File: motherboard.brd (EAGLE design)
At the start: 177.1 x 75.9 mm, 188 parts, among them IC1 LM2576, IC10 TUSB2046B, IC12 LM50, IC13 LM50, IC2 74LS595D, IC3 74LS595D, IC4 IC_FT230X-SSOP-16, IC5 VN5772AK, IC6 VN5772AK, IC7 VN5772AK, IC8 VN5772AK, IC9 VN5772AK, U2 NCP4625, U3 ATMEGA168, Y1 16Mhz, Y2 6MHz

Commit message: laying out subsystems
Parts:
- moved D8 244.7 mm to (-247.7, 204.5), turned to 270 degrees
- moved JP2 242.3 mm to (-213.4, 219.7)
- moved JP3 241.3 mm to (-221.0, 219.7)
- moved JP4 240.3 mm to (-228.6, 219.7)
- moved JP5 239.3 mm to (-236.2, 219.7)
- moved JP6 238.3 mm to (-243.8, 219.7)
- moved D9 233.3 mm to (-247.7, 195.6), turned to 270 degrees
- moved C22 226.7 mm to (-243.2, 15.2), turned to 90 degrees
- moved IC9 223.9 mm to (-252.7, 171.4), turned to 270 degrees
- moved IC7 221.3 mm to (-214.6, 166.4)
- moved D10 221.0 mm to (-240.0, 204.5), turned to 270 degrees
- moved IC8 219.8 mm to (-231.1, 167.6)
- moved C9 214.5 mm to (-231.1, 24.1)
- moved IC1 214.1 mm to (-85.1, 214.6)
- moved U2 211.3 mm to (-240.0, 15.2)
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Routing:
- net GND: track 0.00 -> 107.7 mm, vias 0 -> 69
- net +12V: track 0.00 -> 95.9 mm, vias 0 -> 5
- net +5V: track 0.00 -> 33.4 mm
- net 3.3V: track 0.00 -> 20.4 mm
- net N$5: track 0.00 -> 19.6 mm
- net N$13: track 0.00 -> 19.6 mm
- net N$15: track 0.00 -> 19.6 mm
- net N$12: track 0.00 -> 19.6 mm
- net N$9: track 0.00 -> 19.6 mm
- net N$10: track 0.00 -> 17.2 mm
- net N$11: track 0.00 -> 17.2 mm
- net N$3: track 0.00 -> 17.1 mm
- net N$8: track 0.00 -> 17.1 mm
- net N$14: track 0.00 -> 17.1 mm
- net N$1: track 0.00 -> 9.35 mm
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- added copper zone on layer 1, net GND

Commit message: updated
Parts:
- added C43: 0.1uF, adafruit:C1206
- moved C52 223.6 mm to (-236.2, 29.5), turned to 180 degrees
- moved IC4 219.3 mm to (-236.2, 22.9), turned to 270 degrees
- moved R27 218.5 mm to (-231.1, 22.9), turned to 270 degrees
- moved C23 217.0 mm to (-241.3, 21.3), turned to 270 degrees
- moved R29 215.5 mm to (-236.2, 18.7), turned to 180 degrees
- moved R30 212.0 mm to (-236.2, 16.2), turned to 180 degrees
- moved R28 211.5 mm to (-228.6, 22.9), turned to 270 degrees
- moved C34 198.3 mm to (-236.2, 27.0), turned to 180 degrees
- moved R11 195.2 mm to (-200.0, 21.3)
- moved C32 171.4 mm to (-232.1, 17.5), turned to 270 degrees
- moved IC3 163.3 mm to (-132.1, 200.3), turned to 270 degrees
- moved C33 159.5 mm to (-229.9, 27.0), turned to 180 degrees
- moved C37 147.7 mm to (-132.1, 222.9), turned to 180 degrees
- moved C7 146.4 mm to (-132.1, 220.3), turned to 180 degrees
- moved U$13 144.8 mm to (-134.6, 47.0), turned to 180 degrees
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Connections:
- new net N$16: C43.2, IC4.2
- net !RST: now also C43.1; no longer IC4.2
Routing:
- net +5V: track 33.4 -> 127.4 mm, vias 0 -> 3
- net MISO: track 0.00 -> 30.9 mm
- net D1+: track 0.00 -> 30.9 mm, vias 0 -> 2
- net SCK: track 0.00 -> 30.7 mm
- net MOSI: track 0.00 -> 30.7 mm
- net D1-: track 0.00 -> 26.0 mm, vias 0 -> 2
- net N$26: track 0.00 -> 23.7 mm
- net N$27: track 0.00 -> 20.9 mm, vias 0 -> 2
- net AGND: track 0.00 -> 18.3 mm
- net GND: track 107.7 -> 90.2 mm
- net N$19: track 0.00 -> 13.3 mm
- net N$38: track 0.00 -> 9.87 mm
- net N$7: track 0.00 -> 9.27 mm
- net N$51: track 0.00 -> 8.29 mm
- net N$58: track 0.00 -> 8.29 mm
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
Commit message: rewired h-bridges to not short out and simplified trace layout
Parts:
- moved C21 271.8 mm to (-290.8, 135.9)
- moved C19 251.1 mm to (-261.6, 144.8)
- moved C11 240.6 mm to (-284.5, 231.1)
- moved C13 229.8 mm to (-276.9, 231.1)
- moved C40 208.3 mm to (-283.2, 135.9)
- moved C15 205.6 mm to (-284.5, 188.0)
- moved C42 194.7 mm to (-275.6, 135.9)
- moved C17 193.7 mm to (-276.9, 188.0)
- moved R7 144.7 mm to (-290.8, 224.8)
- moved C10 143.0 mm to (-288.3, 252.7)
- moved R8 137.4 mm to (-285.8, 224.8)
- moved ZD2 134.9 mm to (-290.8, 231.1)
- moved D20 115.2 mm to (-289.6, 118.1), turned to 0 degrees
- moved IC6 110.9 mm to (-284.5, 240.0), turned to 0 degrees
- moved R9 107.8 mm to (-285.8, 181.6)
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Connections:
- removed net N$15: C41.2, D8.A, D9.C, IC9.12, IC9.14, IC9.15, IC9.18, IC9.22, IC9.23, JP6.2
- new net N$59: C6.1, D2.A, D3.C, IC5.1, IC5.22, IC5.23, IC5.25, IC5.28, IC5.3, JP2.1
- net 1HA: now also IC7.2, IC7.8; no longer IC6.2, IC6.8
- net 1HB: now also IC7.13, IC7.7; no longer IC6.13, IC6.7
- net 1SENSE: now also R10.1, R9.2, ZD3.C; no longer R7.2, R8.1, ZD2.C
- net 1STAT: now also IC7.4; no longer IC6.4
- net 2HA: now also IC6.2, IC6.8; no longer IC7.2, IC7.8
- net 2HB: now also IC6.13, IC6.7; no longer IC7.13, IC7.7
- net 2SENSE: now also R7.2, R8.1, ZD2.C; no longer R10.1, R9.2, ZD3.C
- net 2STAT: now also IC6.4; no longer IC7.4
- net 3HA: now also IC9.2, IC9.8; no longer IC8.2, IC8.8
- net 3HB: now also IC9.13, IC9.7; no longer IC8.13, IC8.7
- net 3SENSE: now also R36.2, R37.1, ZD5.C; no longer R26.2, R31.1, ZD4.C
- net 3STAT: now also IC9.4; no longer IC8.4
- net 4HA: now also IC8.2, IC8.8; no longer IC9.2, IC9.8
- net 4HB: now also IC8.13, IC8.7; no longer IC9.13, IC9.7
- net 4SENSE: now also R26.2, R31.1, ZD4.C; no longer R36.2, R37.1, ZD5.C
- net 4STAT: now also IC8.4; no longer IC9.4
- net N$10: now also C20.2, D16.A, D17.C, IC8.12, IC8.14, IC8.15, IC8.18, JP5.2; no longer C20.1, D10.A, D11.C, IC8.1, IC8.25, IC8.28, IC8.3, JP5.1
- net N$11: now also C20.1, D14.A, D15.C, IC8.1, IC8.22, IC8.23, IC8.25, IC8.28, IC8.3, JP5.1; no longer C6.1, D2.A, D3.C, IC5.1, IC5.20, IC5.21, IC5.25, IC5.28, IC5.3, JP2.1
- net N$12: now also C41.2, D20.A, D21.C, IC9.12, IC9.14, IC9.15, IC9.18, IC9.20, IC9.21, JP6.2; no longer C20.2, D12.A, D13.C, IC8.12, IC8.14, IC8.15, IC8.18, IC8.22, IC8.23, JP5.2
- net N$13: now also IC5.20, IC5.21; no longer IC5.22, IC5.23
- net N$14: now also D18.A, D19.C, IC9.22, IC9.23; no longer D6.A, D7.C, IC9.20, IC9.21
- net N$3: now also C12.2, D8.A, D9.C, IC6.12, IC6.14, IC6.15, IC6.18, JP3.2; no longer C12.1, D18.A, D19.C, IC6.1, IC6.25, IC6.28, IC6.3, JP3.1
- net N$5: now also C12.1, D6.A, D7.C, IC6.1, IC6.25, IC6.28, IC6.3, JP3.1; no longer C12.2, D20.A, D21.C, IC6.12, IC6.14, IC6.15, IC6.18, JP3.2
- net N$8: now also C16.2, D12.A, D13.C, IC7.12, IC7.14, IC7.15, IC7.18, JP4.2; no longer C16.1, D14.A, D15.C, IC7.1, IC7.25, IC7.28, IC7.3, JP4.1
- net N$9: now also C16.1, D10.A, D11.C, IC7.1, IC7.25, IC7.28, IC7.3, JP4.1; no longer C16.2, D16.A, D17.C, IC7.12, IC7.14, IC7.15, IC7.18, JP4.2
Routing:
- net N$5: track 19.6 -> 0.00 mm
- net N$15: track 19.6 -> 0.00 mm
- net N$12: track 19.6 -> 0.00 mm
- net N$9: track 19.6 -> 0.00 mm
- net N$10: track 17.2 -> 0.00 mm
- net N$59: track 0.00 -> 17.2 mm
- net N$11: track 17.2 -> 0.00 mm
- net N$3: track 17.1 -> 0.00 mm
- net N$8: track 17.1 -> 0.00 mm
- net N$14: track 17.1 -> 0.00 mm
- net +12V: track 95.9 -> 79.4 mm
- net GND: track 90.2 -> 74.2 mm

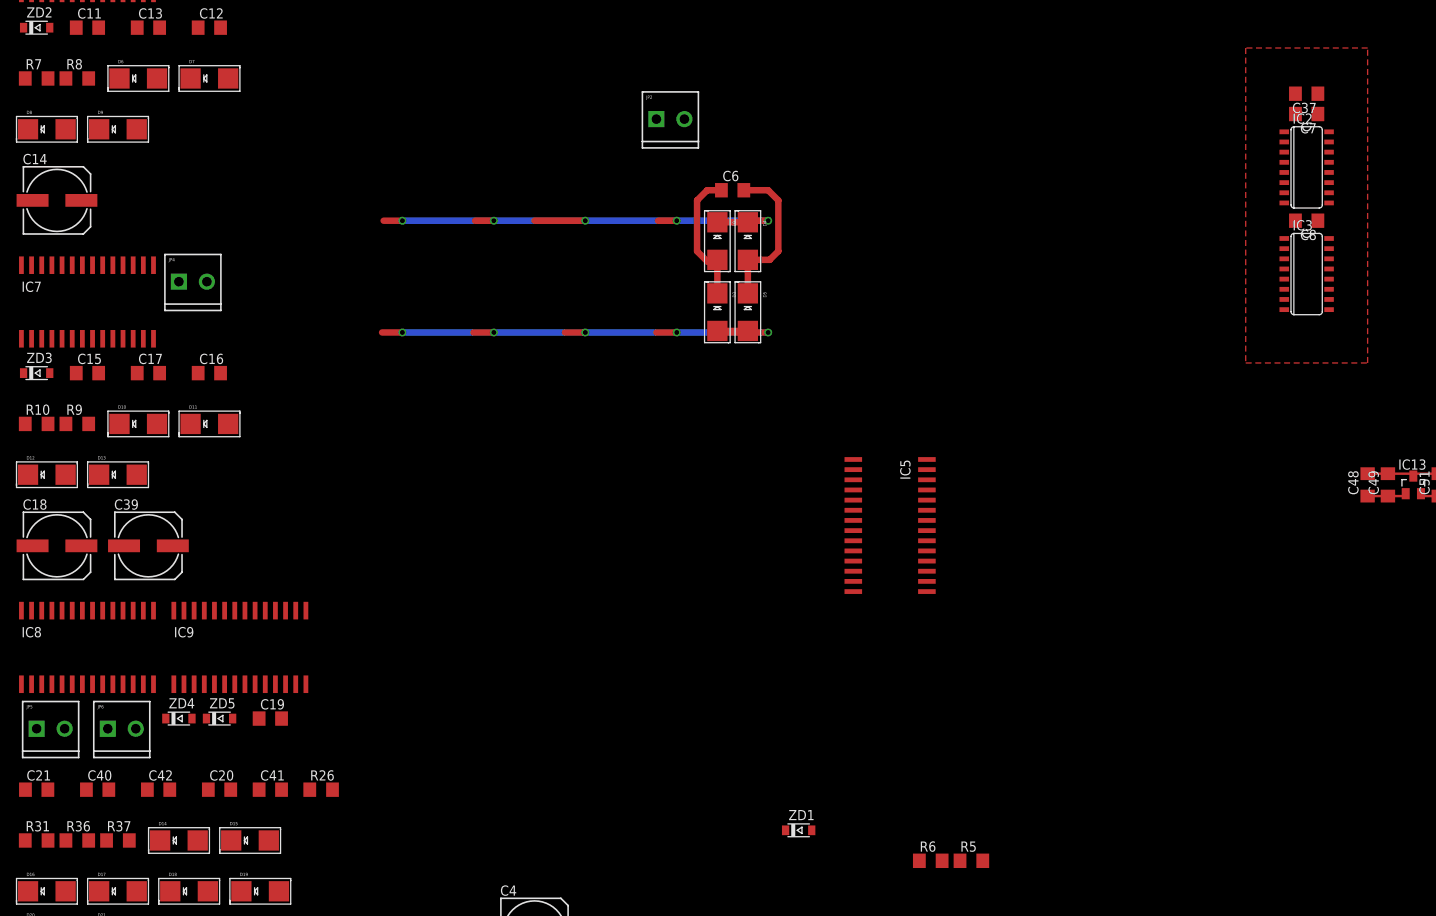
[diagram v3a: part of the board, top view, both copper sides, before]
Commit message: added current liminting resistors to shift registers
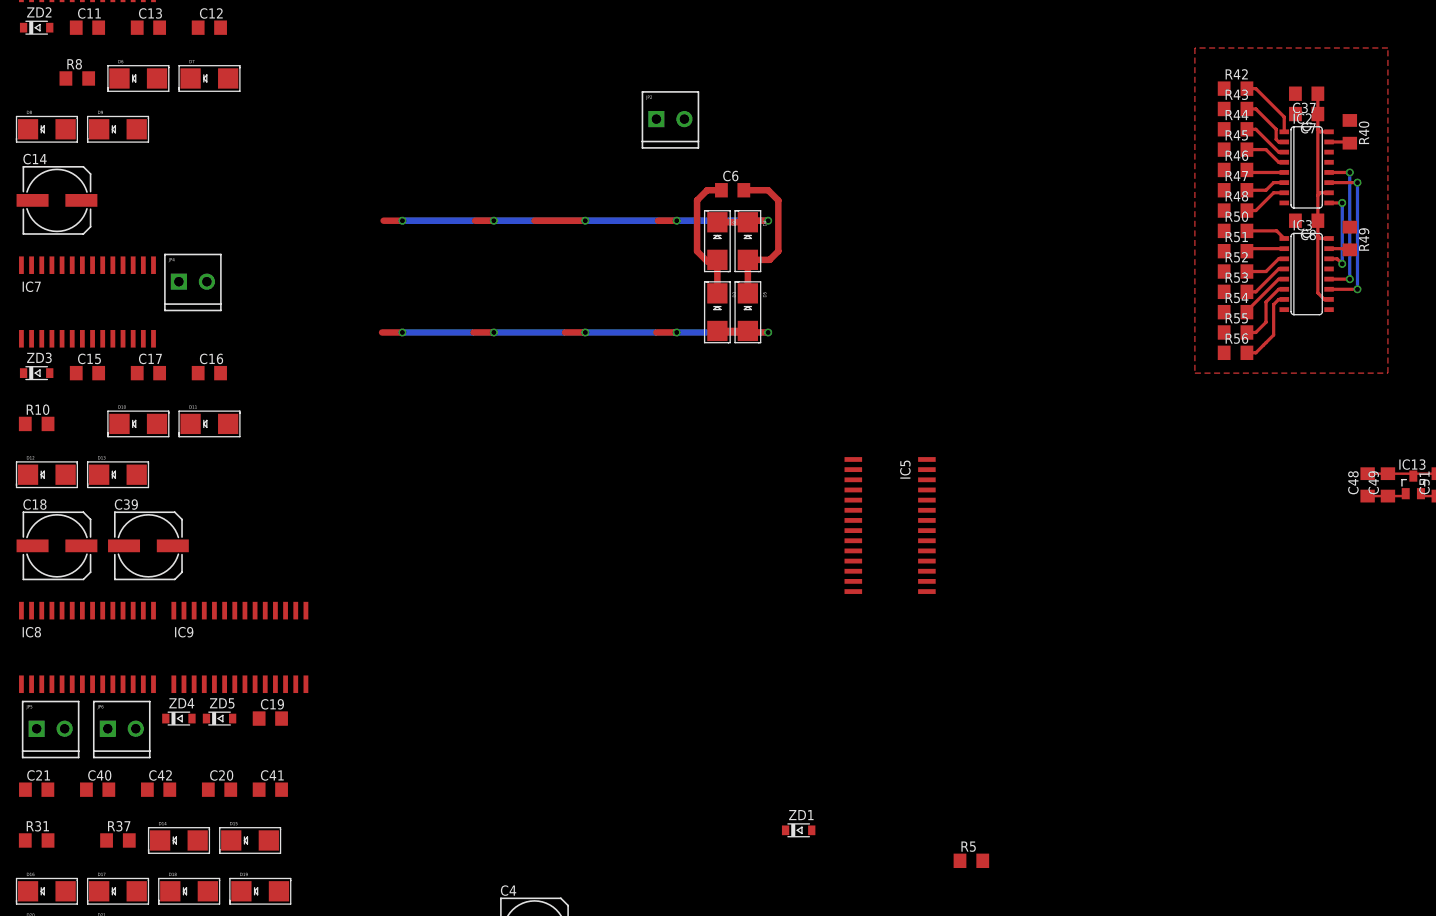
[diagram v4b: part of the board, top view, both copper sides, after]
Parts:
- removed R26, R36, R6, R7, R9: 1k, adafruit:R1206
- added R40, R42, R43, R44, R45, R46, R47, R48, R49, R50, R51, R52, R53, R54, R55, R56: 10k, adafruit:R1206
- R10, R31, R37, R5, R8: value 1k -> 2k
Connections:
- removed net 5HA: IC3.2
- removed net 5HB: IC3.3
- new net N$15: IC3.7, R56.2
- new net N$17: IC3.6, R55.2
- new net N$18: IC3.5, R54.2
- new net N$56: IC3.4, R53.2
- new net N$60: IC3.3, R52.2
- new net N$61: IC3.2, R51.2
- new net N$62: IC3.1, R50.2
- new net N$63: IC3.15, R49.2
- new net N$64: IC2.7, R48.2
- new net N$65: IC2.6, R47.2
- new net N$66: IC2.5, R46.2
- new net N$67: IC2.4, R45.2
- new net N$68: IC2.3, R44.2
- new net N$69: IC2.2, R43.2
- new net N$70: IC2.1, R42.2
- new net N$71: IC2.15, R40.2
- new net SW4: R54.1, R55.1
- new net SW5: R56.1
- net 0HA: now also R40.1; no longer IC2.15
- net 0HB: now also R42.1; no longer IC2.1
- net 0SENSE: no longer IC6.9, IC7.9, IC8.9, IC9.9, R26.1, R36.1, R6.1, R6.2, R7.1, R9.1
- net 1HA: now also R43.1; no longer IC2.2
- net 1HB: now also R44.1; no longer IC2.3
- net 1SENSE: now also IC7.9; no longer R9.2
- net 2HA: now also R45.1; no longer IC2.4
- net 2HB: now also R46.1; no longer IC2.5
- net 2SENSE: now also IC6.9; no longer R7.2
- net 3HA: now also R47.1; no longer IC2.6
- net 3HB: now also R48.1; no longer IC2.7
- net 3SENSE: now also IC9.9; no longer R36.2
- net 4HA: now also R49.1; no longer IC3.15
- net 4HB: now also R50.1; no longer IC3.1
- net 4SENSE: now also IC8.9; no longer R26.2
- net SW0: now also R51.1; no longer IC3.4
- net SW1: now also R52.1; no longer IC3.5
- net SW2: now also R53.1; no longer IC3.6
- net SW3: no longer IC3.7
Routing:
- net +5V: track 127.4 -> 158.6 mm
- net SCK: track 30.7 -> 51.2 mm, vias 0 -> 2
- net LATCH: track 0.00 -> 18.5 mm, vias 0 -> 2
- net N$6: track 0.00 -> 11.2 mm, vias 0 -> 2
- net N$15: track 0.00 -> 9.66 mm
- net N$17: track 0.00 -> 8.39 mm
- net N$70: track 0.00 -> 7.99 mm
- net N$69: track 0.00 -> 7.12 mm
- net N$18: track 0.00 -> 6.47 mm
- net N$68: track 0.00 -> 5.85 mm
- net N$56: track 0.00 -> 5.85 mm
- net N$64: track 0.00 -> 5.59 mm
- net N$67: track 0.00 -> 5.33 mm
- net N$60: track 0.00 -> 5.33 mm
- net N$65: track 0.00 -> 5.06 mm
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
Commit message: laying out protection diodes
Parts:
- added C44, C45: 1000uF, adafruit:153CLV-0807
- added F4, F9: (no value), special:FUSE1
- added JP11, JP12: (no value), sparkfun:SCREWTERMINAL-3.5MM-2
- added Q5, Q6: (no value), adafruit:SOT23
- added R26, R36, R6, R7, R9: 70, adafruit:R1206
- added U$19, U$20: TVS, sparkfun:SMA-DIODE
- R11: value (none) -> 1.5k
- moved D16 95.2 mm to (-240.0, 204.5), turned to 270 degrees
- moved D20 94.4 mm to (-251.5, 204.5), turned to 270 degrees
- moved JP5 92.7 mm to (-236.2, 218.4), turned to 180 degrees
- moved D18 84.8 mm to (-247.7, 204.5), turned to 270 degrees
- moved D14 83.5 mm to (-236.2, 204.5), turned to 270 degrees
- moved D17 83.0 mm to (-240.0, 195.6), turned to 270 degrees
- moved D21 82.8 mm to (-251.5, 195.6), turned to 270 degrees
- moved JP6 82.4 mm to (-247.7, 218.4), turned to 180 degrees
- moved C20 80.7 mm to (-238.1, 210.8), turned to 180 degrees
- moved C41 75.9 mm to (-249.6, 210.8), turned to 180 degrees
- moved D19 74.0 mm to (-247.7, 195.6), turned to 270 degrees
- moved D8 73.7 mm to (-217.2, 204.5), turned to 270 degrees
- moved D15 71.7 mm to (-236.2, 195.6), turned to 270 degrees
- moved D6 67.9 mm to (-213.4, 204.5), turned to 270 degrees
- moved D12 67.6 mm to (-228.6, 204.5), turned to 270 degrees
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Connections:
- new net N$72: JP11.2, Q5.3
- new net N$73: JP12.2, Q6.3
- new net N$74: C45.+, F9.1A, JP12.1, U$20.C
- new net N$75: C44.+, F4.1A, JP11.1, U$19.C
- new net N$76: IC5.9, R6.2
- new net N$77: IC7.9, R7.2
- new net N$78: IC6.9, R9.2
- new net N$79: IC9.9, R36.2
- new net N$80: IC8.9, R26.2
- net +12V: now also F4.2A, F9.2A
- net 0SENSE: now also R6.1; no longer IC5.9
- net 1SENSE: now also R7.1; no longer IC7.9
- net 2SENSE: now also R9.1; no longer IC6.9
- net 3SENSE: now also R36.1; no longer IC9.9
- net 4SENSE: now also R26.1; no longer IC8.9
- net GND: now also C44.-, C45.-, Q5.2, Q6.2, U$19.A, U$20.A
- net SW4: now also Q5.1
- net SW5: now also Q6.1
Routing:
- net N$5: track 0.00 -> 34.0 mm
- net N$9: track 0.00 -> 34.0 mm
- net N$14: track 0.00 -> 34.0 mm
- net N$11: track 0.00 -> 34.0 mm
- net N$3: track 0.00 -> 31.4 mm
- net N$8: track 0.00 -> 31.4 mm
- net N$10: track 0.00 -> 31.4 mm
- net N$12: track 0.00 -> 31.4 mm
- net N$59: track 17.2 -> 34.0 mm
- net +12V: track 79.4 -> 94.6 mm
- net GND: track 74.2 -> 89.1 mm
- net N$13: track 19.6 -> 31.4 mm

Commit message: laying out hbridges
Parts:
- moved C5 292.5 mm to (-295.9, 275.6), turned to 180 degrees
- moved C38 291.1 mm to (-295.9, 278.1), turned to 180 degrees
- moved R5 183.9 mm to (-278.8, 278.1), turned to 90 degrees
- moved C4 183.5 mm to (-297.2, 288.3), turned to 270 degrees
- moved ZD1 168.1 mm to (-276.5, 278.1), turned to 90 degrees
- moved IC5 155.1 mm to (-283.2, 288.3), turned to 0 degrees
- moved R6 84.5 mm to (-281.3, 278.1), turned to 90 degrees
- moved R36 64.8 mm to (-280.7, 114.3)
- moved C39 48.9 mm to (-299.7, 123.2), turned to 270 degrees
- moved R26 43.7 mm to (-284.5, 144.8)
- moved R9 42.7 mm to (-292.1, 224.8), turned to 180 degrees
- moved ZD5 37.8 mm to (-280.7, 109.2)
- moved IC9 36.6 mm to (-285.8, 123.2)
- moved C42 28.5 mm to (-285.8, 109.2)
- moved C40 21.7 mm to (-285.8, 114.3)
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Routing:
- net +12V: track 94.6 -> 193.6 mm
- net N$9: track 34.0 -> 61.8 mm
- net N$8: track 31.4 -> 59.2 mm
- net N$13: track 31.4 -> 58.0 mm
- net N$11: track 34.0 -> 60.5 mm
- net N$5: track 34.0 -> 60.5 mm
- net N$10: track 31.4 -> 58.0 mm
- net N$3: track 31.4 -> 58.0 mm
- net N$59: track 34.0 -> 60.5 mm
- net 0HB: track 0.00 -> 13.1 mm, vias 0 -> 2
- net 0HA: track 0.00 -> 11.8 mm, vias 0 -> 2
- net GND: vias 69 -> 240

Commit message: laying out components
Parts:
- moved C23 276.5 mm to (34.6, 2.54), turned to 0 degrees
- moved R30 276.0 mm to (39.7, 7.62), turned to 270 degrees
- moved R29 273.6 mm to (37.1, 7.62), turned to 270 degrees
- moved C43 271.6 mm to (29.2, 2.54), turned to 0 degrees
- moved C32 270.6 mm to (38.4, 11.7), turned to 0 degrees
- moved IC4 269.7 mm to (33.0, 7.62), turned to 0 degrees
- moved C34 265.8 mm to (28.9, 7.62), turned to 270 degrees
- moved R27 264.4 mm to (33.0, 12.7), turned to 0 degrees
- moved C52 263.5 mm to (26.4, 7.62), turned to 270 degrees
- moved L4 262.1 mm to (20.0, 4.76), turned to 180 degrees
- moved R28 261.7 mm to (33.0, 15.2), turned to 0 degrees
- moved C22 259.1 mm to (33.0, 17.8), turned to 180 degrees
- moved C33 259.1 mm to (28.9, 14.0), turned to 270 degrees
- moved C25 256.5 mm to (20.0, 9.84), turned to 270 degrees
- moved U2 255.9 mm to (33.0, 21.0), turned to 90 degrees
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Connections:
- net SW3: now also R54.1
- net SW4: no longer R54.1
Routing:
- net +12V: track 193.6 -> 297.8 mm
- net N$14: track 34.0 -> 69.2 mm
- net N$12: track 31.4 -> 66.3 mm
- net N$44: track 5.56 -> 32.4 mm
- net N$50: track 0.00 -> 22.3 mm
- net N$20: track 0.00 -> 22.3 mm
- net N$75: track 0.00 -> 22.3 mm
- net N$74: track 0.00 -> 22.3 mm
- net N$54: track 0.00 -> 22.3 mm
- net N$55: track 0.00 -> 22.3 mm
- net N$45: track 5.70 -> 27.7 mm
- net N$30: track 2.78 -> 23.5 mm, vias 0 -> 2
- net N$31: track 2.78 -> 21.8 mm
- net N$13: track 58.0 -> 72.8 mm
- net N$59: track 60.5 -> 74.0 mm
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- added copper zone on layer 16, net GND

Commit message: changing h bridge layout
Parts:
- moved F7 246.1 mm to (-216.2, 201.9), turned to 180 degrees
- moved F8 243.2 mm to (-216.2, 191.8), turned to 180 degrees
- moved F5 241.0 mm to (-216.2, 181.6), turned to 180 degrees
- moved F6 239.8 mm to (-216.2, 171.4), turned to 180 degrees
- moved F9 239.8 mm to (-216.2, 151.1), turned to 180 degrees
- moved F4 239.3 mm to (-216.2, 161.3), turned to 180 degrees
- moved C55 221.3 mm to (-198.1, 201.9), turned to 180 degrees
- moved C56 218.0 mm to (-198.1, 191.8), turned to 180 degrees
- moved C53 215.7 mm to (-198.1, 181.6), turned to 180 degrees
- moved C45 214.2 mm to (-198.1, 151.1), turned to 180 degrees
- moved C54 214.2 mm to (-198.1, 171.4), turned to 180 degrees
- moved C44 213.7 mm to (-198.1, 161.3), turned to 180 degrees
- moved U$8 211.7 mm to (-190.5, 203.8), turned to 90 degrees
- moved Q3 209.8 mm to (-190.5, 198.8), turned to 270 degrees
- moved U$9 208.1 mm to (-190.5, 193.7), turned to 90 degrees
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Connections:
- net AGND: now also R10.2, R31.2, R37.2, R5.2, R8.2, ZD1.A, ZD2.A, ZD3.A, ZD4.A, ZD5.A
- net GND: no longer R10.2, R31.2, R37.2, R5.2, R8.2, ZD1.A, ZD2.A, ZD3.A, ZD4.A, ZD5.A
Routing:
- net +12V: track 297.8 -> 370.2 mm
- net 4HB: track 0.00 -> 13.1 mm, vias 0 -> 2
- net 1HB: track 0.00 -> 13.0 mm, vias 0 -> 2
- net 3HB: track 0.00 -> 13.0 mm, vias 0 -> 2
- net 2HB: track 0.00 -> 13.0 mm, vias 0 -> 2
- net 4HA: track 0.00 -> 11.9 mm, vias 0 -> 2
- net 3HA: track 0.00 -> 11.1 mm, vias 0 -> 2
- net 2HA: track 0.00 -> 11.1 mm, vias 0 -> 2
- net 1HA: track 0.00 -> 11.1 mm, vias 0 -> 2
- net N$25: track 10.2 -> 14.3 mm
- net GND: track 97.5 -> 95.5 mm
- net 0HA: track 11.8 -> 11.1 mm
